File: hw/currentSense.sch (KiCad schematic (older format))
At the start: 4 parts, among them U601 ZXCT1086

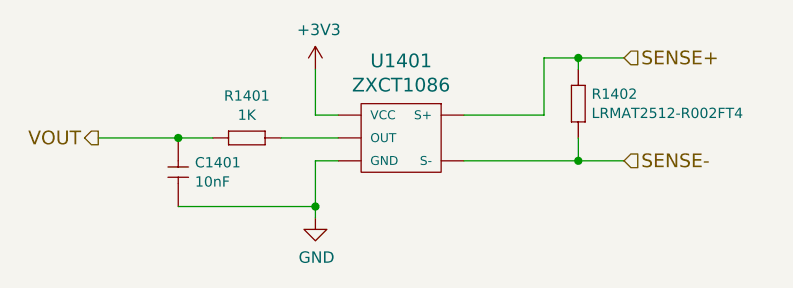
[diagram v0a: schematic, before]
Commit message: added 1k pull down resistors to mosfet gates
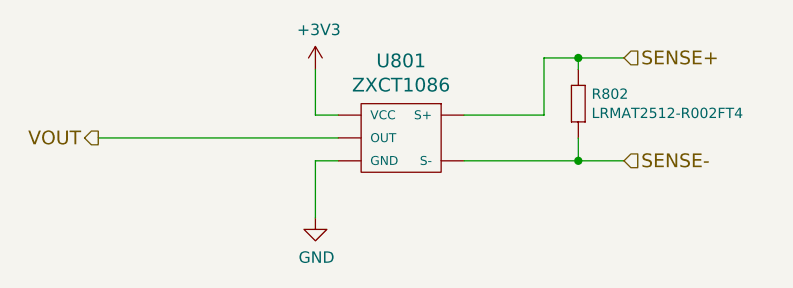
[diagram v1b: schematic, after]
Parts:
- removed C801: 10nF, kemet:0603, symbol 10nF
- removed R801: 1K, multicomp:0603, symbol 1K
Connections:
- net VOUT: now also U601.1 (OUT)
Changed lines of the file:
@@
 $Descr A4 11693 8268
 encoding utf-8
-Sheet 7 16
+Sheet 8 16
 Title "MSB current sense sheet"
 Date "2017-02-05"
@@
 AR Path="/58C7B0A8/58BE8E88/589841A1" Ref="U1301"  Part="1"
 AR Path="/58C7B0A8/58BE8E96/589841A1" Ref="U1401"  Part="1"
-F 0 "U1401" H 5425 3887 60  0000 C CNN
+F 0 "U801" H 5425 3887 60  0000 C CNN
 F 1 "ZXCT1086" H 5425 3781 60  0000 C CNN
 F 2 "usevolt:SOT-25" H 5100 4050 60  0001 C CNN
@@
 AR Path="/58C7B0A8/58BE8E88/589841A8" Ref="#PWR1302"  Part="1"
 AR Path="/58C7B0A8/58BE8E96/589841A8" Ref="#PWR1402"  Part="1"
-F 0 "#PWR1402" H 5050 3750 50  0001 C CNN
+F 0 "#PWR802" H 5050 3750 50  0001 C CNN
 F 1 "GND" H 5055 3827 50  0000 C CNN
 F 2 "" H 5050 4000 50  0000 C CNN
@@
 AR Path="/58C7B0A8/58BE8E88/589841AE" Ref="#PWR1301"  Part="1"
 AR Path="/58C7B0A8/58BE8E96/589841AE" Ref="#PWR1401"  Part="1"
-F 0 "#PWR1401" H 5050 3200 50  0001 C CNN
+F 0 "#PWR801" H 5050 3200 50  0001 C CNN
 F 1 "+3V3" H 5065 3523 50  0000 C CNN
 F 2 "" H 5050 3350 50  0000 C CNN
@@
 	1    5050 3350
 	1    0    0    -1
-$EndComp
-$Comp
-L 1K R?
-U 1 1 589841B8
-P 4700 3650
-AR Path="/589841B8" Ref="R?"  Part="1"
-AR Path="/58982E87/589841B8" Ref="R?"  Part="1"
-AR Path="/5899DD67/589841B8" Ref="R?"  Part="1"
-AR Path="/589A417E/589841B8" Ref="R?"  Part="1"
-AR Path="/58BE52C9/58BE8E88/589841B8" Ref="R801"  Part="1"
-AR Path="/58BE52C9/58BE8E4D/589841B8" Ref="R601"  Part="1"
-AR Path="/58BE52C9/58BE8E7A/589841B8" Ref="R701"  Part="1"
-AR Path="/58BE52C9/58BE8E96/589841B8" Ref="R901"  Part="1"
-AR Path="/58C7B0A8/58BE8E4D/589841B8" Ref="R1101"  Part="1"
-AR Path="/58C7B0A8/58BE8E7A/589841B8" Ref="R1201"  Part="1"
-AR Path="/58C7B0A8/58BE8E88/589841B8" Ref="R1301"  Part="1"
-AR Path="/58C7B0A8/58BE8E96/589841B8" Ref="R1401"  Part="1"
-F 0 "R1401" H 4750 3834 45  0000 C CNN
-F 1 "1K" H 4750 3750 45  0000 C CNN
-F 2 "multicomp:0603" H 4730 3800 20  0001 C CNN
-F 3 "" H 4669 3689 60  0001 C CNN
-F 4 "9330380" H 5069 4089 60  0001 C CNN "1st Source Part Number"
-F 5 "Farnell" H 4969 3989 60  0001 C CNN "1st Source"
-F 6 "MC0063W060311K" H 4869 3889 60  0001 C CNN "Manufacturer Part Number"
-F 7 "MULTICOMP" H 4769 3789 60  0001 C CNN "Manufacturer"
-	1    4700 3650
-	1    0    0    -1
-$EndComp
-$Comp
-L 10nF C?
-U 1 1 589841C3
-P 4450 3750
-AR Path="/589841C3" Ref="C?"  Part="1"
-AR Path="/58982E87/589841C3" Ref="C?"  Part="1"
-AR Path="/5899DD67/589841C3" Ref="C?"  Part="1"
-AR Path="/589A417E/589841C3" Ref="C?"  Part="1"
-AR Path="/58BE52C9/58BE8E88/589841C3" Ref="C801"  Part="1"
-AR Path="/58BE52C9/58BE8E4D/589841C3" Ref="C601"  Part="1"
-AR Path="/58BE52C9/58BE8E7A/589841C3" Ref="C701"  Part="1"
-AR Path="/58BE52C9/58BE8E96/589841C3" Ref="C901"  Part="1"
-AR Path="/58C7B0A8/58BE8E4D/589841C3" Ref="C1101"  Part="1"
-AR Path="/58C7B0A8/58BE8E7A/589841C3" Ref="C1201"  Part="1"
-AR Path="/58C7B0A8/58BE8E88/589841C3" Ref="C1301"  Part="1"
-AR Path="/58C7B0A8/58BE8E96/589841C3" Ref="C1401"  Part="1"
-F 0 "C1401" V 4458 3823 45  0000 L CNN
-F 1 "10nF" V 4542 3823 45  0000 L CNN
-F 2 "kemet:0603" H 4480 3900 20  0001 C CNN
-F 3 "http://www.farnell.com/datasheets/2064086.pdf?_ga=1.250530118.1948984246.1460023966" H 4354 3759 60  0001 C CNN
-F 4 "1457729" H 4754 4159 60  0001 C CNN "1st Source Part Number"
-F 5 "C0603C103J3GACTU" H 4554 3959 60  0001 C CNN "Manufacturer Part Number"
-F 6 "Farnell" H 4654 4059 60  0001 C CNN "1st Source"
-F 7 "KEMET" H 4454 3859 60  0001 C CNN "Manufacturer"
-	1    4450 3750
-	0    1    1    0
 $EndComp
 Wire Wire Line
@@
 	5050 3550 5150 3550
 Wire Wire Line
-	4900 3650 5150 3650
-Wire Wire Line
-	4100 3650 4600 3650
-Wire Wire Line
-	5050 3950 4450 3950
-Connection ~ 5050 3950
-Connection ~ 4450 3650
+	4100 3650 5150 3650
 Text HLabel 6400 3300 2    60   Input ~ 0
 SENSE+
@@
 AR Path="/58C7B0A8/58BE8E88/589858BC" Ref="R1302"  Part="1"
 AR Path="/58C7B0A8/58BE8E96/589858BC" Ref="R1402"  Part="1"
-F 0 "R1402" V 6208 3508 45  0000 L CNN
+F 0 "R802" V 6208 3508 45  0000 L CNN
 F 1 "LRMAT2512-R002FT4" V 6292 3508 45  0000 L CNN
 F 2 "usevolt:2512" H 6230 3600 20  0001 C CNN

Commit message: pcb first revision created, ready to order
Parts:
- renumbered R802 to R601
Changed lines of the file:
@@
 EESchema Schematic File Version 2
-LIBS:msb-rescue
 LIBS:kemet
 LIBS:multicomp
@@
 LIBS:power
 LIBS:elt21300_kicad
-LIBS:msb-cache
+LIBS:esb-cache
 EELAYER 26 0
 EELAYER END
 $Descr A4 11693 8268
 encoding utf-8
-Sheet 8 16
+Sheet 11 17
 Title "MSB current sense sheet"
 Date "2017-02-05"
@@
 $Comp
 L ZXCT1086 U601
-U 1 1 589841A1
+U 1 1 594D8B7D
 P 5450 3600
-AR Path="/58BE52C9/58BE8E4D/589841A1" Ref="U601"  Part="1"
-AR Path="/58BE52C9/58BE8E7A/589841A1" Ref="U701"  Part="1"
-AR Path="/58BE52C9/58BE8E88/589841A1" Ref="U801"  Part="1"
-AR Path="/58BE52C9/58BE8E96/589841A1" Ref="U901"  Part="1"
-AR Path="/58C7B0A8/58BE8E4D/589841A1" Ref="U1101"  Part="1"
-AR Path="/58C7B0A8/58BE8E7A/589841A1" Ref="U1201"  Part="1"
-AR Path="/58C7B0A8/58BE8E88/589841A1" Ref="U1301"  Part="1"
-AR Path="/58C7B0A8/58BE8E96/589841A1" Ref="U1401"  Part="1"
-F 0 "U801" H 5425 3887 60  0000 C CNN
+AR Path="/58BE52C9/58BE8E4D/594D8B7D" Ref="U601"  Part="1"
+AR Path="/58BE52C9/58BE8E7A/594D8B7D" Ref="U701"  Part="1"
+AR Path="/58BE52C9/5955DE03/594D8B7D" Ref="U801"  Part="1"
+AR Path="/58C7B0A8/594D8B80/594D8B7D" Ref="U1001"  Part="1"
+AR Path="/58C7B0A8/594D8B83/594D8B7D" Ref="U1101"  Part="1"
+AR Path="/58C7B0A8/58BE8E88/594D8B7D" Ref="U1201"  Part="1"
+F 0 "U1201" H 5425 3887 60  0000 C CNN
 F 1 "ZXCT1086" H 5425 3781 60  0000 C CNN
 F 2 "usevolt:SOT-25" H 5100 4050 60  0001 C CNN
@@
 $Comp
 L GND #PWR602
-U 1 1 589841A8
+U 1 1 594D8B7E
 P 5050 4000
-AR Path="/58BE52C9/58BE8E4D/589841A8" Ref="#PWR602"  Part="1"
-AR Path="/58BE52C9/58BE8E7A/589841A8" Ref="#PWR702"  Part="1"
-AR Path="/58BE52C9/58BE8E88/589841A8" Ref="#PWR802"  Part="1"
-AR Path="/58BE52C9/58BE8E96/589841A8" Ref="#PWR902"  Part="1"
-AR Path="/58C7B0A8/58BE8E4D/589841A8" Ref="#PWR1102"  Part="1"
-AR Path="/58C7B0A8/58BE8E7A/589841A8" Ref="#PWR1202"  Part="1"
-AR Path="/58C7B0A8/58BE8E88/589841A8" Ref="#PWR1302"  Part="1"
-AR Path="/58C7B0A8/58BE8E96/589841A8" Ref="#PWR1402"  Part="1"
-F 0 "#PWR802" H 5050 3750 50  0001 C CNN
+AR Path="/58BE52C9/58BE8E4D/594D8B7E" Ref="#PWR602"  Part="1"
+AR Path="/58BE52C9/58BE8E7A/594D8B7E" Ref="#PWR702"  Part="1"
+AR Path="/58BE52C9/5955DE03/594D8B7E" Ref="#PWR802"  Part="1"
+AR Path="/58C7B0A8/594D8B80/594D8B7E" Ref="#PWR1002"  Part="1"
+AR Path="/58C7B0A8/594D8B83/594D8B7E" Ref="#PWR1102"  Part="1"
+AR Path="/58C7B0A8/58BE8E88/594D8B7E" Ref="#PWR1202"  Part="1"
+F 0 "#PWR1202" H 5050 3750 50  0001 C CNN
 F 1 "GND" H 5055 3827 50  0000 C CNN
 F 2 "" H 5050 4000 50  0000 C CNN
@@
 AR Path="/58BE52C9/58BE8E4D/589841AE" Ref="#PWR601"  Part="1"
 AR Path="/58BE52C9/58BE8E7A/589841AE" Ref="#PWR701"  Part="1"
-AR Path="/58BE52C9/58BE8E88/589841AE" Ref="#PWR801"  Part="1"
-AR Path="/58BE52C9/58BE8E96/589841AE" Ref="#PWR901"  Part="1"
-AR Path="/58C7B0A8/58BE8E4D/589841AE" Ref="#PWR1101"  Part="1"
-AR Path="/58C7B0A8/58BE8E7A/589841AE" Ref="#PWR1201"  Part="1"
-AR Path="/58C7B0A8/58BE8E88/589841AE" Ref="#PWR1301"  Part="1"
-AR Path="/58C7B0A8/58BE8E96/589841AE" Ref="#PWR1401"  Part="1"
-F 0 "#PWR801" H 5050 3200 50  0001 C CNN
+AR Path="/58BE52C9/5955DE03/589841AE" Ref="#PWR801"  Part="1"
+AR Path="/58C7B0A8/594D8B80/589841AE" Ref="#PWR1001"  Part="1"
+AR Path="/58C7B0A8/594D8B83/589841AE" Ref="#PWR1101"  Part="1"
+AR Path="/58C7B0A8/58BE8E88/589841AE" Ref="#PWR1201"  Part="1"
+F 0 "#PWR1201" H 5050 3200 50  0001 C CNN
 F 1 "+3V3" H 5065 3523 50  0000 C CNN
 F 2 "" H 5050 3350 50  0000 C CNN
@@
 AR Path="/5899DD67/589858BC" Ref="R?"  Part="1"
 AR Path="/589A417E/589858BC" Ref="R?"  Part="1"
-AR Path="/58BE52C9/58BE8E88/589858BC" Ref="R802"  Part="1"
-AR Path="/58BE52C9/58BE8E4D/589858BC" Ref="R602"  Part="1"
-AR Path="/58BE52C9/58BE8E7A/589858BC" Ref="R702"  Part="1"
-AR Path="/58BE52C9/58BE8E96/589858BC" Ref="R902"  Part="1"
-AR Path="/58C7B0A8/58BE8E4D/589858BC" Ref="R1102"  Part="1"
-AR Path="/58C7B0A8/58BE8E7A/589858BC" Ref="R1202"  Part="1"
-AR Path="/58C7B0A8/58BE8E88/589858BC" Ref="R1302"  Part="1"
-AR Path="/58C7B0A8/58BE8E96/589858BC" Ref="R1402"  Part="1"
-F 0 "R802" V 6208 3508 45  0000 L CNN
+AR Path="/58BE52C9/58BE8E88/589858BC" Ref="R?"  Part="1"
+AR Path="/58BE52C9/58BE8E4D/589858BC" Ref="R601"  Part="1"
+AR Path="/58BE52C9/58BE8E7A/589858BC" Ref="R701"  Part="1"
+AR Path="/58BE52C9/58BE8E96/589858BC" Ref="R?"  Part="1"
+AR Path="/58C7B0A8/58BE8E4D/589858BC" Ref="R?"  Part="1"
+AR Path="/58C7B0A8/58BE8E7A/589858BC" Ref="R?"  Part="1"
+AR Path="/58C7B0A8/58BE8E88/589858BC" Ref="R1201"  Part="1"
+AR Path="/58C7B0A8/58BE8E96/589858BC" Ref="R?"  Part="1"
+AR Path="/58BE52C9/5955DE03/589858BC" Ref="R801"  Part="1"
+AR Path="/58C7B0A8/594D8B80/589858BC" Ref="R1001"  Part="1"
+AR Path="/58C7B0A8/594D8B83/589858BC" Ref="R1101"  Part="1"
+F 0 "R1201" V 6208 3508 45  0000 L CNN
 F 1 "LRMAT2512-R002FT4" V 6292 3508 45  0000 L CNN
 F 2 "usevolt:2512" H 6230 3600 20  0001 C CNN

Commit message: tag 3.0.0 schematic drawing started
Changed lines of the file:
@@
 $EndDescr
 $Comp
-L GND #PWR602
+L GND #PWR029
 U 1 1 594D8B7E
 P 5050 4000
-AR Path="/58BE52C9/58BE8E4D/594D8B7E" Ref="#PWR602"  Part="1"
-AR Path="/58BE52C9/58BE8E7A/594D8B7E" Ref="#PWR702"  Part="1"
-AR Path="/58BE52C9/5955DE03/594D8B7E" Ref="#PWR802"  Part="1"
-AR Path="/58C7B0A8/594D8B80/594D8B7E" Ref="#PWR1002"  Part="1"
-AR Path="/58C7B0A8/594D8B83/594D8B7E" Ref="#PWR1102"  Part="1"
-AR Path="/58C7B0A8/58BE8E88/594D8B7E" Ref="#PWR1202"  Part="1"
-F 0 "#PWR1202" H 5050 3750 50  0001 C CNN
+AR Path="/58BE52C9/58BE8E4D/594D8B7E" Ref="#PWR029"  Part="1"
+AR Path="/58BE52C9/5955DE03/594D8B7E" Ref="#PWR031"  Part="1"
+AR Path="/58BE52C9/59B27EDC/594D8B7E" Ref="#PWR033"  Part="1"
+AR Path="/58C7B0A8/594D8B80/594D8B7E" Ref="#PWR038"  Part="1"
+AR Path="/58C7B0A8/594D8B83/594D8B7E" Ref="#PWR040"  Part="1"
+AR Path="/58C7B0A8/58BE8E88/594D8B7E" Ref="#PWR042"  Part="1"
+F 0 "#PWR042" H 5050 3750 50  0001 C CNN
 F 1 "GND" H 5055 3827 50  0000 C CNN
 F 2 "" H 5050 4000 50  0000 C CNN
@@
 $EndComp
 $Comp
-L +3V3 #PWR601
+L +3V3 #PWR030
 U 1 1 589841AE
 P 5050 3350
-AR Path="/58BE52C9/58BE8E4D/589841AE" Ref="#PWR601"  Part="1"
-AR Path="/58BE52C9/58BE8E7A/589841AE" Ref="#PWR701"  Part="1"
-AR Path="/58BE52C9/5955DE03/589841AE" Ref="#PWR801"  Part="1"
-AR Path="/58C7B0A8/594D8B80/589841AE" Ref="#PWR1001"  Part="1"
-AR Path="/58C7B0A8/594D8B83/589841AE" Ref="#PWR1101"  Part="1"
-AR Path="/58C7B0A8/58BE8E88/589841AE" Ref="#PWR1201"  Part="1"
-F 0 "#PWR1201" H 5050 3200 50  0001 C CNN
+AR Path="/58BE52C9/58BE8E4D/589841AE" Ref="#PWR030"  Part="1"
+AR Path="/58BE52C9/5955DE03/589841AE" Ref="#PWR032"  Part="1"
+AR Path="/58BE52C9/59B27EDC/589841AE" Ref="#PWR034"  Part="1"
+AR Path="/58C7B0A8/594D8B80/589841AE" Ref="#PWR039"  Part="1"
+AR Path="/58C7B0A8/594D8B83/589841AE" Ref="#PWR041"  Part="1"
+AR Path="/58C7B0A8/58BE8E88/589841AE" Ref="#PWR043"  Part="1"
+F 0 "#PWR043" H 5050 3200 50  0001 C CNN
 F 1 "+3V3" H 5065 3523 50  0000 C CNN
 F 2 "" H 5050 3350 50  0000 C CNN
@@
 P 6200 3450
 AR Path="/58BE52C9/58BE8E4D/597AFC4A" Ref="R601"  Part="1"
-AR Path="/58BE52C9/58BE8E7A/597AFC4A" Ref="R701"  Part="1"
-AR Path="/58BE52C9/5955DE03/597AFC4A" Ref="R801"  Part="1"
+AR Path="/58BE52C9/58BE8E7A/597AFC4A" Ref="R?"  Part="1"
+AR Path="/58BE52C9/5955DE03/597AFC4A" Ref="R701"  Part="1"
 AR Path="/58C7B0A8/594D8B80/597AFC4A" Ref="R1001"  Part="1"
 AR Path="/58C7B0A8/594D8B83/597AFC4A" Ref="R1101"  Part="1"
 AR Path="/58C7B0A8/58BE8E88/597AFC4A" Ref="R1201"  Part="1"
-F 0 "R1201" V 6208 3508 45  0000 L CNN
+AR Path="/58BE52C9/59B27EDC/597AFC4A" Ref="R801"  Part="1"
+F 0 "R701" V 6208 3508 45  0000 L CNN
 F 1 "LRMAT2512-R002FT4" V 6292 3508 45  0000 L CNN
 F 2 "usevolt:2512" H 6230 3600 20  0001 C CNN
@@
 P 5450 3600
 AR Path="/58BE52C9/58BE8E4D/597AFC97" Ref="U601"  Part="1"
-AR Path="/58BE52C9/58BE8E7A/597AFC97" Ref="U701"  Part="1"
-AR Path="/58BE52C9/5955DE03/597AFC97" Ref="U801"  Part="1"
+AR Path="/58BE52C9/5955DE03/597AFC97" Ref="U701"  Part="1"
+AR Path="/58BE52C9/59B27EDC/597AFC97" Ref="U801"  Part="1"
 AR Path="/58C7B0A8/594D8B80/597AFC97" Ref="U1001"  Part="1"
 AR Path="/58C7B0A8/594D8B83/597AFC97" Ref="U1101"  Part="1"
 AR Path="/58C7B0A8/58BE8E88/597AFC97" Ref="U1201"  Part="1"
-F 0 "U1201" H 5425 3887 60  0000 C CNN
+F 0 "U701" H 5425 3887 60  0000 C CNN
 F 1 "ZXCT1086" H 5425 3781 60  0000 C CNN
 F 2 "usevolt:SOT-25" H 5100 4050 60  0001 C CNN

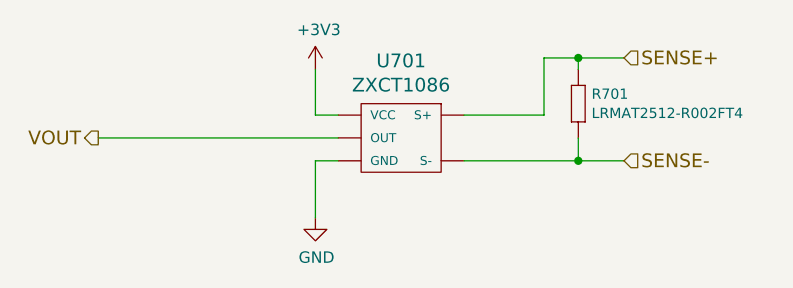
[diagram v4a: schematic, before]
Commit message: added binary and build files to gitignore
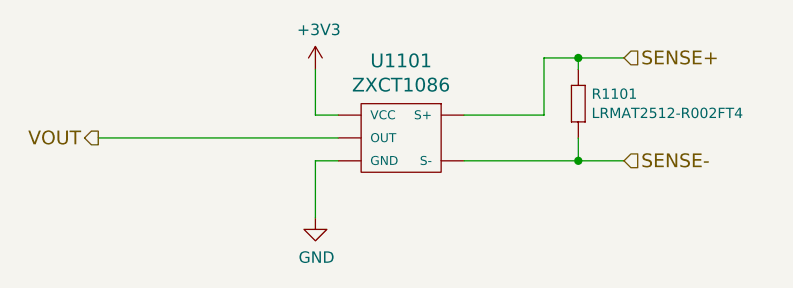
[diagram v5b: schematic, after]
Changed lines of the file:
@@
 $EndDescr
 $Comp
-L GND #PWR029
+L GND #PWR028
 U 1 1 594D8B7E
 P 5050 4000
-AR Path="/58BE52C9/58BE8E4D/594D8B7E" Ref="#PWR029"  Part="1"
-AR Path="/58BE52C9/5955DE03/594D8B7E" Ref="#PWR031"  Part="1"
-AR Path="/58BE52C9/59B27EDC/594D8B7E" Ref="#PWR033"  Part="1"
-AR Path="/58C7B0A8/594D8B80/594D8B7E" Ref="#PWR038"  Part="1"
-AR Path="/58C7B0A8/594D8B83/594D8B7E" Ref="#PWR040"  Part="1"
-AR Path="/58C7B0A8/58BE8E88/594D8B7E" Ref="#PWR042"  Part="1"
-F 0 "#PWR042" H 5050 3750 50  0001 C CNN
+AR Path="/58BE52C9/58BE8E4D/594D8B7E" Ref="#PWR028"  Part="1"
+AR Path="/58C7B0A8/594D8B80/594D8B7E" Ref="#PWR037"  Part="1"
+AR Path="/58C7B0A8/594D8B83/594D8B7E" Ref="#PWR039"  Part="1"
+F 0 "#PWR039" H 5050 3750 50  0001 C CNN
 F 1 "GND" H 5055 3827 50  0000 C CNN
 F 2 "" H 5050 4000 50  0000 C CNN
@@
 $EndComp
 $Comp
-L +3V3 #PWR030
+L +3V3 #PWR029
 U 1 1 589841AE
 P 5050 3350
-AR Path="/58BE52C9/58BE8E4D/589841AE" Ref="#PWR030"  Part="1"
-AR Path="/58BE52C9/5955DE03/589841AE" Ref="#PWR032"  Part="1"
-AR Path="/58BE52C9/59B27EDC/589841AE" Ref="#PWR034"  Part="1"
-AR Path="/58C7B0A8/594D8B80/589841AE" Ref="#PWR039"  Part="1"
-AR Path="/58C7B0A8/594D8B83/589841AE" Ref="#PWR041"  Part="1"
-AR Path="/58C7B0A8/58BE8E88/589841AE" Ref="#PWR043"  Part="1"
-F 0 "#PWR043" H 5050 3200 50  0001 C CNN
+AR Path="/58BE52C9/58BE8E4D/589841AE" Ref="#PWR029"  Part="1"
+AR Path="/58C7B0A8/594D8B80/589841AE" Ref="#PWR038"  Part="1"
+AR Path="/58C7B0A8/594D8B83/589841AE" Ref="#PWR040"  Part="1"
+F 0 "#PWR040" H 5050 3200 50  0001 C CNN
 F 1 "+3V3" H 5065 3523 50  0000 C CNN
 F 2 "" H 5050 3350 50  0000 C CNN
@@
 AR Path="/58BE52C9/58BE8E4D/597AFC4A" Ref="R601"  Part="1"
 AR Path="/58BE52C9/58BE8E7A/597AFC4A" Ref="R?"  Part="1"
-AR Path="/58BE52C9/5955DE03/597AFC4A" Ref="R701"  Part="1"
+AR Path="/58BE52C9/5955DE03/597AFC4A" Ref="R?"  Part="1"
 AR Path="/58C7B0A8/594D8B80/597AFC4A" Ref="R1001"  Part="1"
 AR Path="/58C7B0A8/594D8B83/597AFC4A" Ref="R1101"  Part="1"
-AR Path="/58C7B0A8/58BE8E88/597AFC4A" Ref="R1201"  Part="1"
-AR Path="/58BE52C9/59B27EDC/597AFC4A" Ref="R801"  Part="1"
-F 0 "R701" V 6208 3508 45  0000 L CNN
+AR Path="/58C7B0A8/58BE8E88/597AFC4A" Ref="R?"  Part="1"
+AR Path="/58BE52C9/59B27EDC/597AFC4A" Ref="R?"  Part="1"
+F 0 "R1101" V 6208 3508 45  0000 L CNN
 F 1 "LRMAT2512-R002FT4" V 6292 3508 45  0000 L CNN
 F 2 "usevolt:2512" H 6230 3600 20  0001 C CNN
@@
 P 5450 3600
 AR Path="/58BE52C9/58BE8E4D/597AFC97" Ref="U601"  Part="1"
-AR Path="/58BE52C9/5955DE03/597AFC97" Ref="U701"  Part="1"
-AR Path="/58BE52C9/59B27EDC/597AFC97" Ref="U801"  Part="1"
 AR Path="/58C7B0A8/594D8B80/597AFC97" Ref="U1001"  Part="1"
 AR Path="/58C7B0A8/594D8B83/597AFC97" Ref="U1101"  Part="1"
-AR Path="/58C7B0A8/58BE8E88/597AFC97" Ref="U1201"  Part="1"
-F 0 "U701" H 5425 3887 60  0000 C CNN
+F 0 "U1101" H 5425 3887 60  0000 C CNN
 F 1 "ZXCT1086" H 5425 3781 60  0000 C CNN
 F 2 "usevolt:SOT-25" H 5100 4050 60  0001 C CNN

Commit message: 3.0.0 ready to order
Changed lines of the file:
@@
 EESchema Schematic File Version 2
+LIBS:esb-rescue
 LIBS:kemet
 LIBS:multicomp
@@
 $Descr A4 11693 8268
 encoding utf-8
-Sheet 6 17
+Sheet 10 19
 Title "MSB current sense sheet"
 Date "2017-02-05"
@@
 $EndDescr
 $Comp
-L GND #PWR028
+L GND #PWR602
 U 1 1 594D8B7E
 P 5050 4000
-AR Path="/58BE52C9/58BE8E4D/594D8B7E" Ref="#PWR028"  Part="1"
-AR Path="/58C7B0A8/594D8B80/594D8B7E" Ref="#PWR037"  Part="1"
-AR Path="/58C7B0A8/594D8B83/594D8B7E" Ref="#PWR039"  Part="1"
-F 0 "#PWR039" H 5050 3750 50  0001 C CNN
+F 0 "#PWR602" H 5050 3750 50  0001 C CNN
 F 1 "GND" H 5055 3827 50  0000 C CNN
 F 2 "" H 5050 4000 50  0000 C CNN
@@
 $EndComp
 $Comp
-L +3V3 #PWR029
+L +3V3 #PWR601
 U 1 1 589841AE
 P 5050 3350
-AR Path="/58BE52C9/58BE8E4D/589841AE" Ref="#PWR029"  Part="1"
-AR Path="/58C7B0A8/594D8B80/589841AE" Ref="#PWR038"  Part="1"
-AR Path="/58C7B0A8/594D8B83/589841AE" Ref="#PWR040"  Part="1"
-F 0 "#PWR040" H 5050 3200 50  0001 C CNN
+F 0 "#PWR601" H 5050 3200 50  0001 C CNN
 F 1 "+3V3" H 5065 3523 50  0000 C CNN
 F 2 "" H 5050 3350 50  0000 C CNN
@@
 AR Path="/58BE52C9/58BE8E7A/597AFC4A" Ref="R?"  Part="1"
 AR Path="/58BE52C9/5955DE03/597AFC4A" Ref="R?"  Part="1"
-AR Path="/58C7B0A8/594D8B80/597AFC4A" Ref="R1001"  Part="1"
-AR Path="/58C7B0A8/594D8B83/597AFC4A" Ref="R1101"  Part="1"
+AR Path="/58C7B0A8/594D8B80/597AFC4A" Ref="R?"  Part="1"
+AR Path="/58C7B0A8/594D8B83/597AFC4A" Ref="R?"  Part="1"
 AR Path="/58C7B0A8/58BE8E88/597AFC4A" Ref="R?"  Part="1"
 AR Path="/58BE52C9/59B27EDC/597AFC4A" Ref="R?"  Part="1"
-F 0 "R1101" V 6208 3508 45  0000 L CNN
+F 0 "R601" V 6208 3508 45  0000 L CNN
 F 1 "LRMAT2512-R002FT4" V 6292 3508 45  0000 L CNN
 F 2 "usevolt:2512" H 6230 3600 20  0001 C CNN
@@
 U 1 1 597AFC97
 P 5450 3600
-AR Path="/58BE52C9/58BE8E4D/597AFC97" Ref="U601"  Part="1"
-AR Path="/58C7B0A8/594D8B80/597AFC97" Ref="U1001"  Part="1"
-AR Path="/58C7B0A8/594D8B83/597AFC97" Ref="U1101"  Part="1"
-F 0 "U1101" H 5425 3887 60  0000 C CNN
+F 0 "U601" H 5425 3887 60  0000 C CNN
 F 1 "ZXCT1086" H 5425 3781 60  0000 C CNN
 F 2 "usevolt:SOT-25" H 5100 4050 60  0001 C CNN
